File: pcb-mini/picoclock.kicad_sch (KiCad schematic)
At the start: 68 parts, among them J1 UART, J10 USB, J11 Alt Power, J12 LED_5V, J2 USB_A, J3 UART, J4 xx, J5 Micro_SD_Card_Det1, J6 USB_C_Receptacle, J7 AudioJack2_Ground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

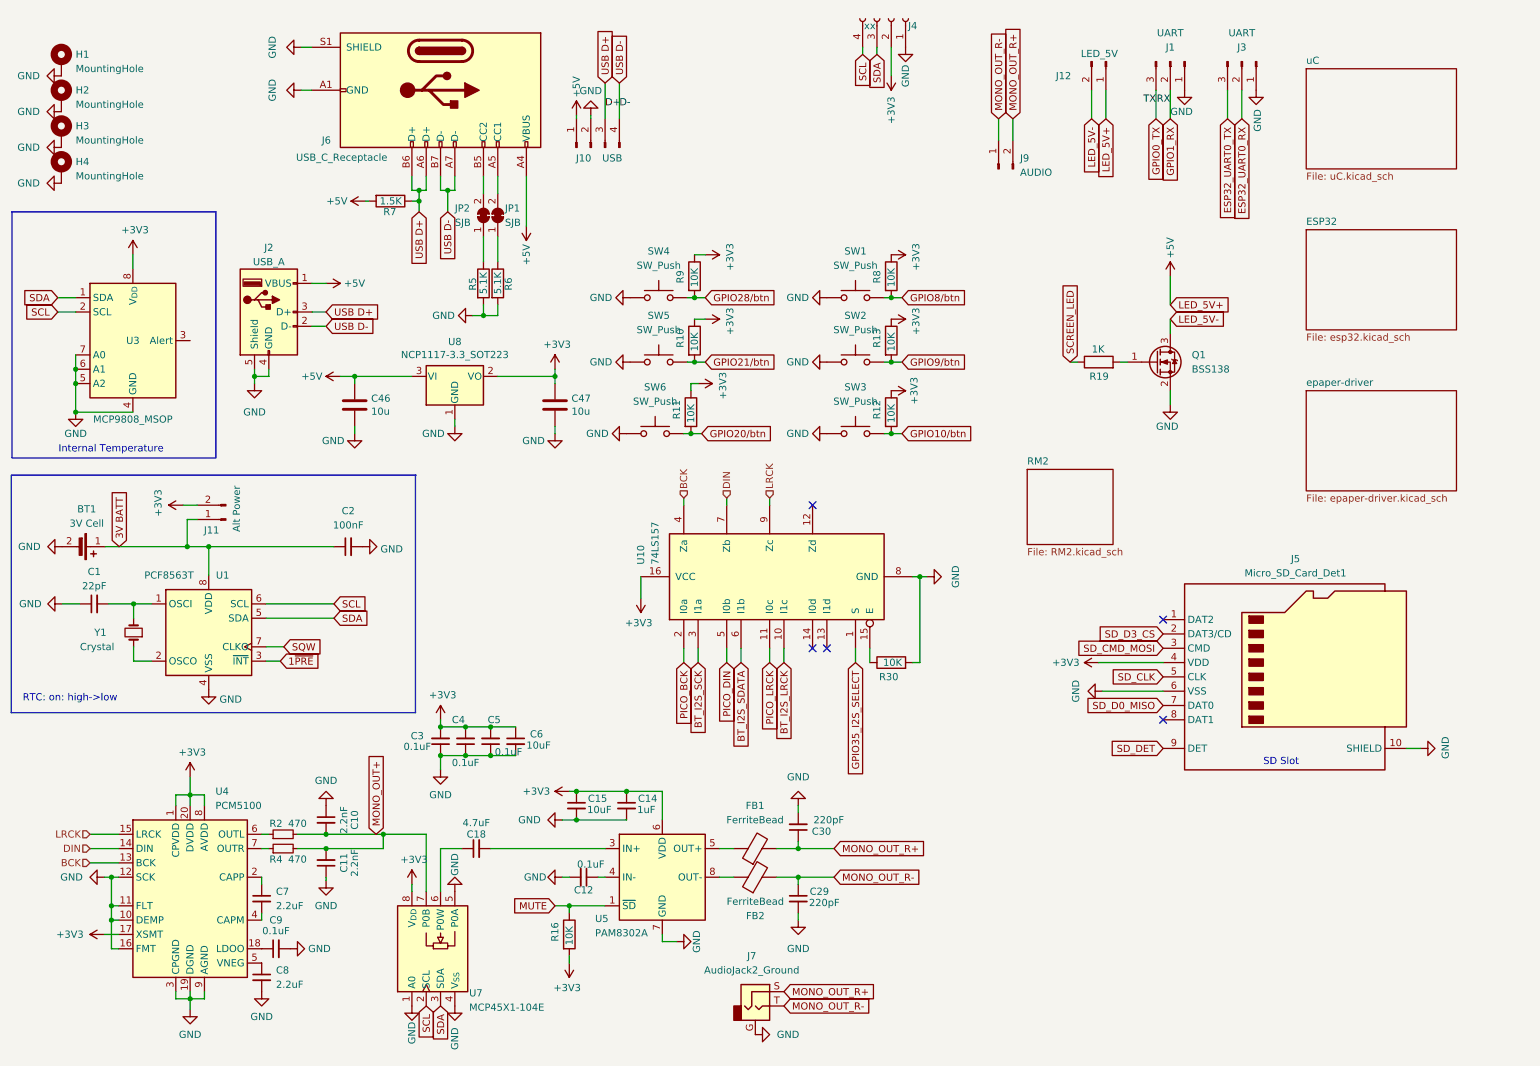
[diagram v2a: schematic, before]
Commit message: [pcb-mini] add proper audio jack
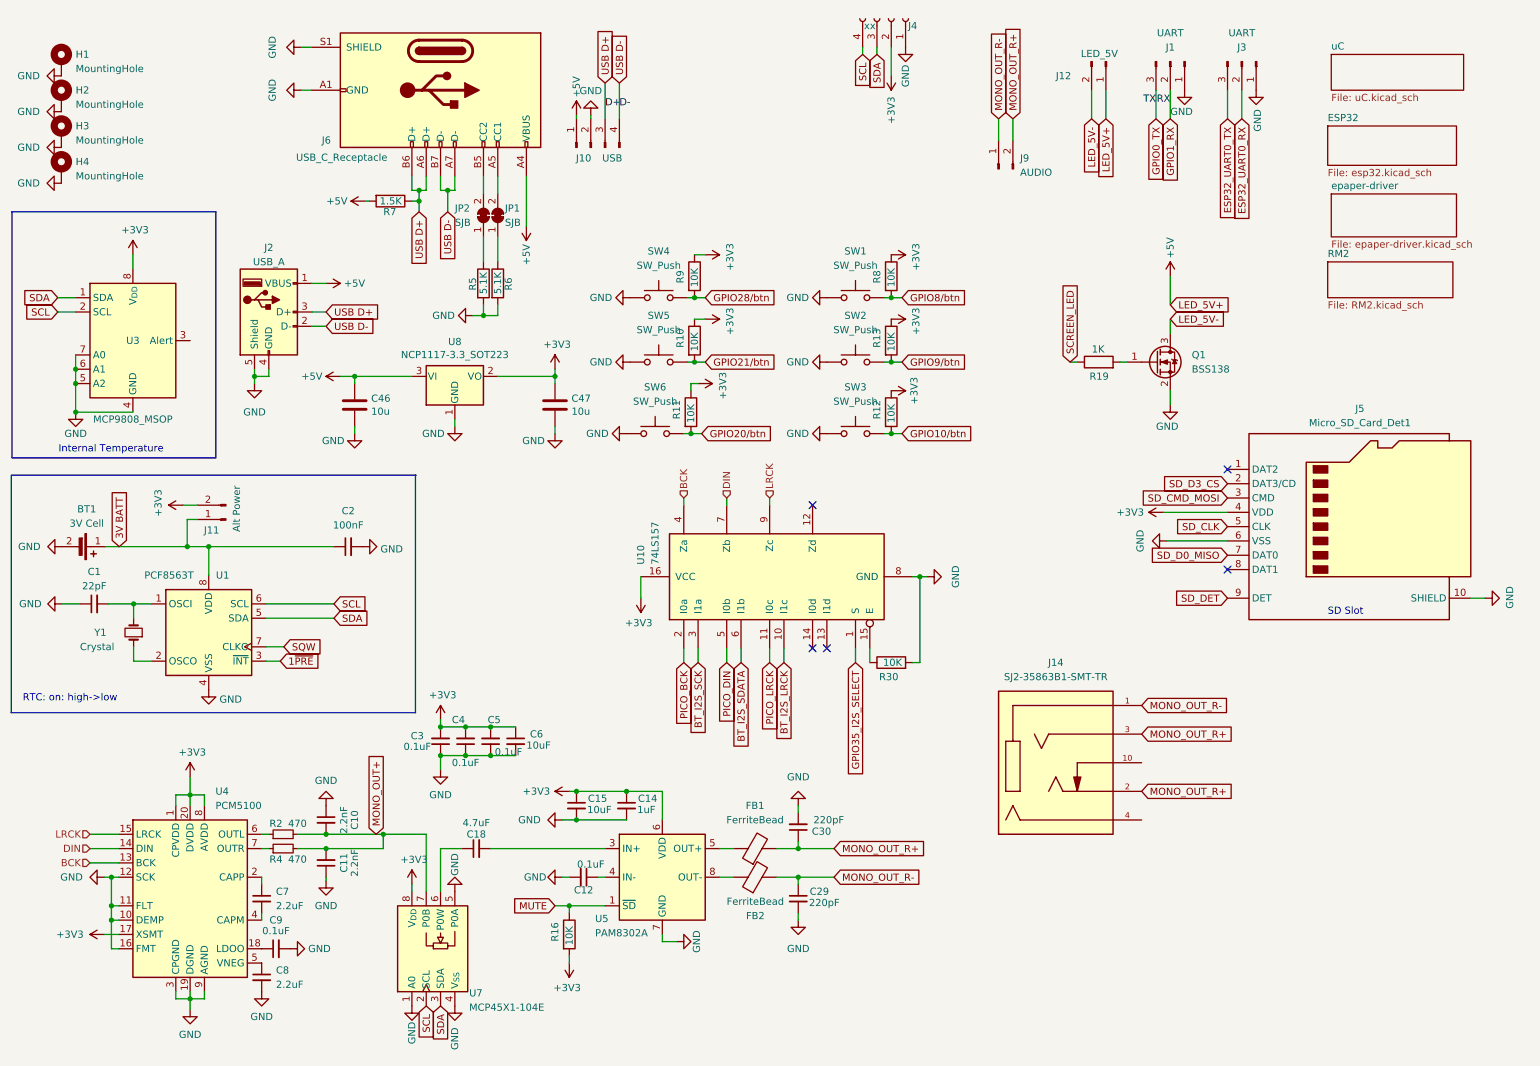
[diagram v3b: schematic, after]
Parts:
- removed J7: AudioJack2_Ground, Connector_Audio:Jack_3.5mm_QingPu_WQP-PJ398SM_Vertical_CircularHoles, symbol Connector_Audio:AudioJack2_Ground
- added J14: SJ2-35863B1-SMT-TR, SJ2-35863B1-SMT-TR:CUI_SJ2-35863B1-SMT-TR, symbol SOP65P780X200-20N:SJ2-35863B1-SMT-TR
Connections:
- net MONO_OUT_R+: now also J14.2, J14.3
- net MONO_OUT_R-: now also J14.1
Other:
- moved on the sheet: J5

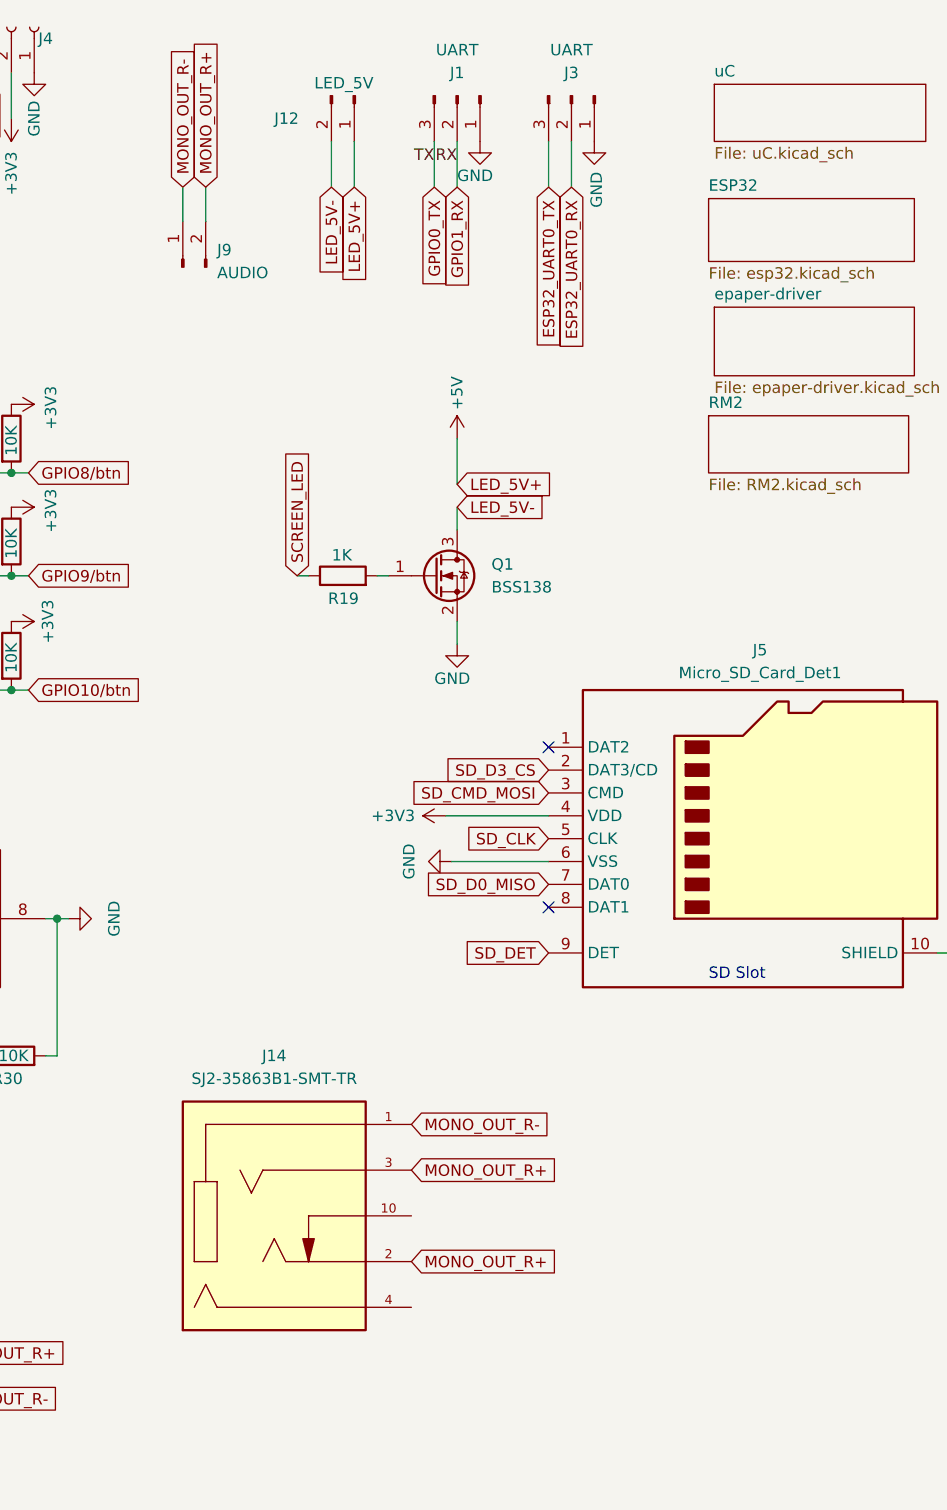
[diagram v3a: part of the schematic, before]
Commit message: [pcb] mini: audio shut internal speaker when hack is connected
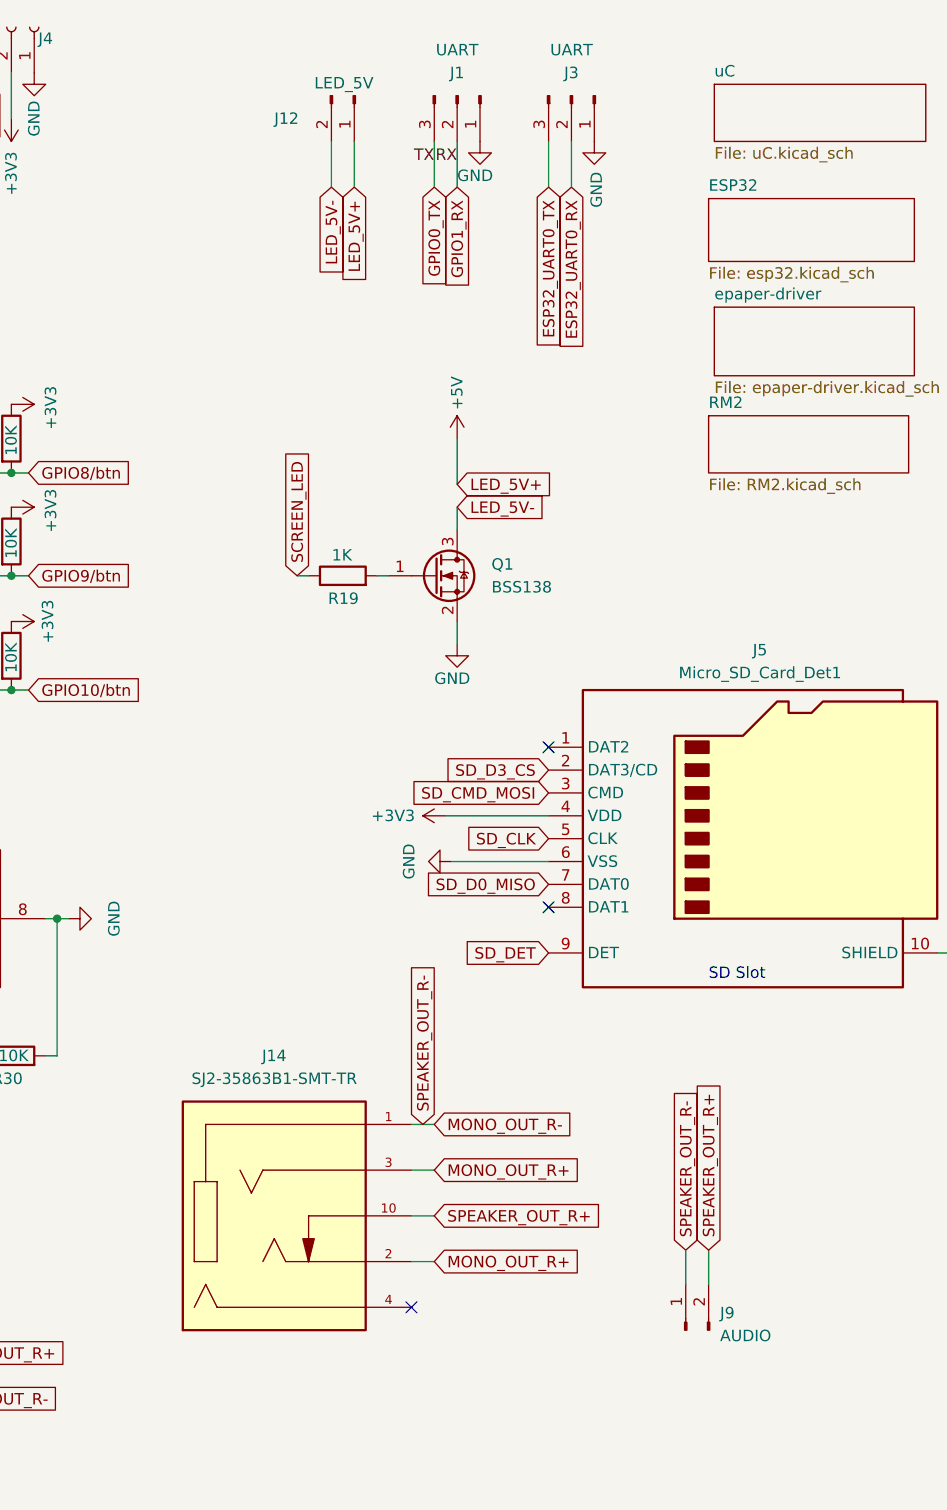
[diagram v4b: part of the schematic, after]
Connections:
- net MONO_OUT_R+: no longer J9.2 (Pin_2)
- net SPEAKER_OUT_R+: now reaches J14.10
- net SPEAKER_OUT_R+: now also J9.2 (Pin_2)
- no-connect marks 5 -> 6
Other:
- moved on the sheet: J9
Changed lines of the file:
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@@
 	)
 	(no_connect
+		(at 214.63 156.21)
+	)
+	(no_connect
 		(at 156.21 125.73)
 	)
@@
 	(wire
 		(pts
-			(xy 45.72 187.96) (xy 45.72 186.69)
+			(xy 217.17 151.13) (xy 214.63 151.13)
 		)
 		(stroke
@@
 	(wire
 		(pts
-			(xy 74.93 78.74) (xy 74.93 77.47)
+			(xy 45.72 187.96) (xy 45.72 186.69)
 		)
 		(stroke
@@
 	(wire
 		(pts
-			(xy 135.255 55.88) (xy 137.16 55.88)
+			(xy 74.93 78.74) (xy 74.93 77.47)
 		)
 		(stroke
@@
 	(wire
 		(pts
-			(xy 191.77 31.75) (xy 191.77 35.56)
+			(xy 135.255 55.88) (xy 137.16 55.88)
 		)
 		(stroke
@@
 	(wire
 		(pts
+			(xy 217.17 140.97) (xy 214.63 140.97)
+		)
+		(stroke
+			(width 0)
+			(type default)
+		)
+	)
+	(wire
+		(pts
 			(xy 90.17 144.78) (xy 94.615 144.78)
 		)
@@
 	(wire
 		(pts
+			(xy 245.11 149.86) (xy 245.11 153.67)
+		)
+		(stroke
+			(width 0)
+			(type default)
+		)
+	)
+	(wire
+		(pts
 			(xy 166.37 128.27) (xy 166.37 125.73)
 		)
@@
 	(wire
 		(pts
+			(xy 247.65 149.86) (xy 247.65 153.67)
+		)
+		(stroke
+			(width 0)
+			(type default)
+		)
+	)
+	(wire
+		(pts
 			(xy 99.06 161.29) (xy 119.38 161.29)
 		)
@@
 	(wire
 		(pts
-			(xy 45.72 148.59) (xy 45.72 151.765)
+			(xy 217.17 146.05) (xy 214.63 146.05)
 		)
 		(stroke
@@
 	(wire
 		(pts
-			(xy 94.615 144.78) (xy 99.06 144.78)
+			(xy 45.72 148.59) (xy 45.72 151.765)
 		)
 		(stroke
@@
 	(wire
 		(pts
-			(xy 48.26 153.67) (xy 48.26 151.765)
+			(xy 94.615 144.78) (xy 99.06 144.78)
 		)
 		(stroke
@@
 	(wire
 		(pts
-			(xy 87.63 44.45) (xy 87.63 41.91)
+			(xy 48.26 153.67) (xy 48.26 151.765)
 		)
 		(stroke
@@
 	(wire
 		(pts
-			(xy 125.73 116.84) (xy 125.73 113.03)
+			(xy 87.63 44.45) (xy 87.63 41.91)
 		)
 		(stroke
@@
 	(wire
 		(pts
-			(xy 189.23 31.75) (xy 189.23 35.56)
+			(xy 125.73 116.84) (xy 125.73 113.03)
 		)
 		(stroke
@@
 	(wire
 		(pts
+			(xy 217.17 135.89) (xy 214.63 135.89)
+		)
+		(stroke
+			(width 0)
+			(type default)
+		)
+	)
+	(wire
+		(pts
 			(xy 64.77 158.75) (xy 69.85 158.75)
 		)
@@
 		)
 	)
+	(global_label "SPEAKER_OUT_R+"
+		(shape input)
+		(at 217.17 146.05 0)
+		(fields_autoplaced yes)
+		(effects
+			(font
+				(size 1.27 1.27)
+			)
+			(justify left)
+		)
+		(property "Intersheetrefs" "${INTERSHEET_REFS}"
+			(at 236.9675 146.05 0)
+			(effects
+				(font
+					(size 1.27 1.27)
+				)
+				(justify left)
+				(hide yes)
+			)
+		)
+	)
 	(global_label "GPIO10{slash}btn"
 		(shape input)
@@
 		)
 	)
+	(global_label "SPEAKER_OUT_R-"
+		(shape input)
+		(at 245.11 149.86 90)
+		(fields_autoplaced yes)
+		(effects
+			(font
+				(size 1.27 1.27)
+			)
+			(justify left)
+		)
+		(property "Intersheetrefs" "${INTERSHEET_REFS}"
+			(at 245.11 130.0625 90)
+			(effects
+				(font
+					(size 1.27 1.27)
+				)
+				(justify left)
+				(hide yes)
+			)
+		)
+	)
 	(global_label "SCL"
 		(shape input)
@@
 		)
 	)
-	(global_label "GPIO8{slash}btn"
+	(global_label "SPEAKER_OUT_R-"
 		(shape input)
-		(at 172.085 63.5 0)
+		(at 215.9 135.89 90)
 		(fields_autoplaced yes)
 		(effects
@@
 		)
 		(property "Intersheetrefs" "${INTERSHEET_REFS}"
-			(at 185.1092 63.5 0)
+			(at 215.9 116.0925 90)
 			(effects
 				(font
@@
 		)
 	)
-	(global_label "MONO_OUT_R-"
+	(global_label "GPIO8{slash}btn"
 		(shape input)
-		(at 189.23 31.75 90)
+		(at 172.085 63.5 0)
 		(fields_autoplaced yes)
 		(effects
@@
 		)
 		(property "Intersheetrefs" "${INTERSHEET_REFS}"
-			(at 189.23 14.9157 90)
+			(at 185.1092 63.5 0)
 			(effects
 				(font
@@
 	(global_label "MONO_OUT_R-"
 		(shape input)
-		(at 214.63 135.89 0)
+		(at 217.17 135.89 0)
 		(fields_autoplaced yes)
 		(effects
@@
 		)
 		(property "Intersheetrefs" "${INTERSHEET_REFS}"
-			(at 231.4643 135.89 0)
+			(at 234.0043 135.89 0)
 			(effects
 				(font
@@
 		)
 	)
-	(global_label "MONO_OUT_R+"
-		(shape input)
-		(at 191.77 31.75 90)
-		(fields_autoplaced yes)
-		(effects
-			(font
-				(size 1.27 1.27)
-			)
-			(justify left)
-		)
-		(property "Intersheetrefs" "${INTERSHEET_REFS}"
-			(at 191.77 14.9157 90)
-			(effects
-				(font
-					(size 1.27 1.27)
-				)
-				(justify left)
-				(hide yes)
-			)
-		)
-	)
 	(global_label "ESP32_UART0_RX"
 		(shape input)
@@
 	(global_label "MONO_OUT_R+"
 		(shape input)
-		(at 214.63 151.13 0)
+		(at 217.17 151.13 0)
 		(fields_autoplaced yes)
 		(effects
@@
 		)
 		(property "Intersheetrefs" "${INTERSHEET_REFS}"
-			(at 231.4643 151.13 0)
+			(at 234.0043 151.13 0)
 			(effects
 				(font
@@
 		)
 	)
+	(global_label "SPEAKER_OUT_R+"
+		(shape input)
+		(at 247.65 149.86 90)
+		(fields_autoplaced yes)
+		(effects
+			(font
+				(size 1.27 1.27)
+			)
+			(justify left)
+		)
+		(property "Intersheetrefs" "${INTERSHEET_REFS}"
+			(at 247.65 130.0625 90)
+			(effects
+				(font
+					(size 1.27 1.27)
+				)
+				(justify left)
+				(hide yes)
+			)
+		)
+	)
 	(global_label "LED_5V-"
 		(shape input)
@@
 	(global_label "MONO_OUT_R+"
 		(shape input)
-		(at 214.63 140.97 0)
+		(at 217.17 140.97 0)
 		(fields_autoplaced yes)
 		(effects
@@
 		)
 		(property "Intersheetrefs" "${INTERSHEET_REFS}"
-			(at 231.4643 140.97 0)
+			(at 234.0043 140.97 0)
 			(effects
 				(font
@@
 	(symbol
 		(lib_id "Connector:Conn_01x02_Pin")
-		(at 189.23 40.64 90)
+		(at 245.11 158.75 90)
 		(unit 1)
 		(exclude_from_sim no)
@@
 		(fields_autoplaced yes)
 		(property "Reference" "J9"
-			(at 193.04 38.7349 90)
+			(at 248.92 156.8449 90)
 			(effects
 				(font
@@
 		)
 		(property "Value" "AUDIO"
-			(at 193.04 41.2749 90)
+			(at 248.92 159.3849 90)
 			(effects
 				(font
@@
 		)
 		(property "Footprint" "Connector_PinHeader_2.54mm:PinHeader_1x02_P2.54mm_Vertical"
-			(at 189.23 40.64 0)
+			(at 245.11 158.75 0)
 			(effects
 				(font
@@
 		)
 		(property "Datasheet" "~"
-			(at 189.23 40.64 0)
+			(at 245.11 158.75 0)
 			(effects
 				(font
@@
 		)
 		(property "Description" "Generic connector, single row, 01x02, script generated"
-			(at 189.23 40.64 0)
+			(at 245.11 158.75 0)
 			(effects
 				(font

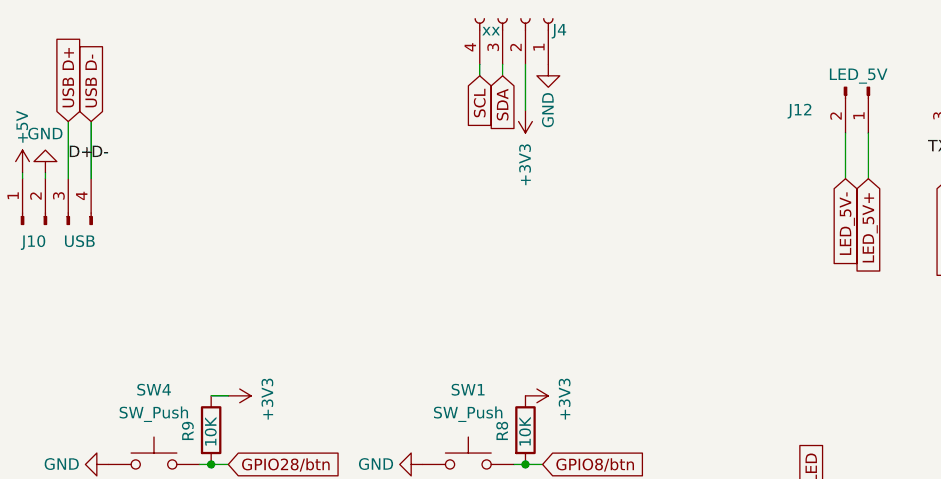
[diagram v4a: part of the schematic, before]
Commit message: [pcb] add leds
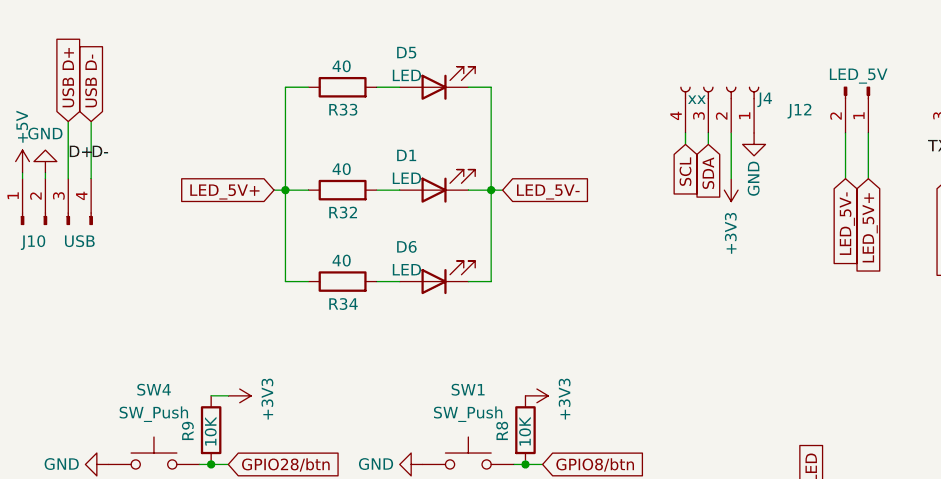
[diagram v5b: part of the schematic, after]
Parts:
- added D1, D5, D6: LED, LED_SMD:LED_PLCC_2835, symbol Device:LED
- added R32, R33, R34: 40, Resistor_SMD:R_0603_1608Metric, symbol Device:R
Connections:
- net +5V: now also R32.1, R33.1, R34.1
- net LED_5V-: now also D1.1 (K), D5.1 (K), D6.1 (K)
- new net: D6.2 (A), R34.2
- new net: D1.2 (A), R32.2
- new net: D5.2 (A), R33.2
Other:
- moved on the sheet: J4
